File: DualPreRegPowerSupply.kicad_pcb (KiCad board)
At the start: 4 copper layers, 100 x 100 mm, 178 parts, among them J101 Banana_Red, J102 Banana_Black, J201 Banana_Red, J202 Banana_Black, J401 Conn_02x05_Odd_Even, J601 Power Input, J801 Conn_01x03_Pin, J802 Conn_02x02_Odd_Even, J901 Power Input, M401 Fan_4pin, Q301 MMBT3904, Q302 TIP42C, Q303 BSS138, Q401 BSS138, Q501 MMBT3906, Q801 BSS138, Q802 BSS138, U1001 AP64060QWU, U1002 AP7383, U1003 LM2776, U1005 XC6901D121MR-G, U301 TLV4387PWR, U302 LMV331, U501 LT8612, U701 ADS1118IDGS, U702 MCP48FVB22, U801 ISO6721RFBD, U802 ATtiny1614-SS, U901 AP63200WU

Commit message: test commit
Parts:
- removed the Q302 at (137.1, 126.6)

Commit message: test commit 2
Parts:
- moved TP504 15.1 mm to (103.2, 68.2)
- moved TP602 5.25 mm to (102.6, 82.6)
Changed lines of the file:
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@@
 	(footprint "LibEigen:SMD Test Point PCWCTE"
 		(layer "B.Cu")
-		(at 97.6 84.1 90)
+		(at 102.625 82.575 90)
 		(property "Reference" "TP602"
 			(at 0 1.9 270)
@@
 	(footprint "LibEigen:SMD Test Point PCWCTE"
 		(layer "B.Cu")
-		(at 92.6 57.5 -90)
+		(at 103.225 68.175 -90)
 		(property "Reference" "TP504"
 			(at 0 1.9 90)

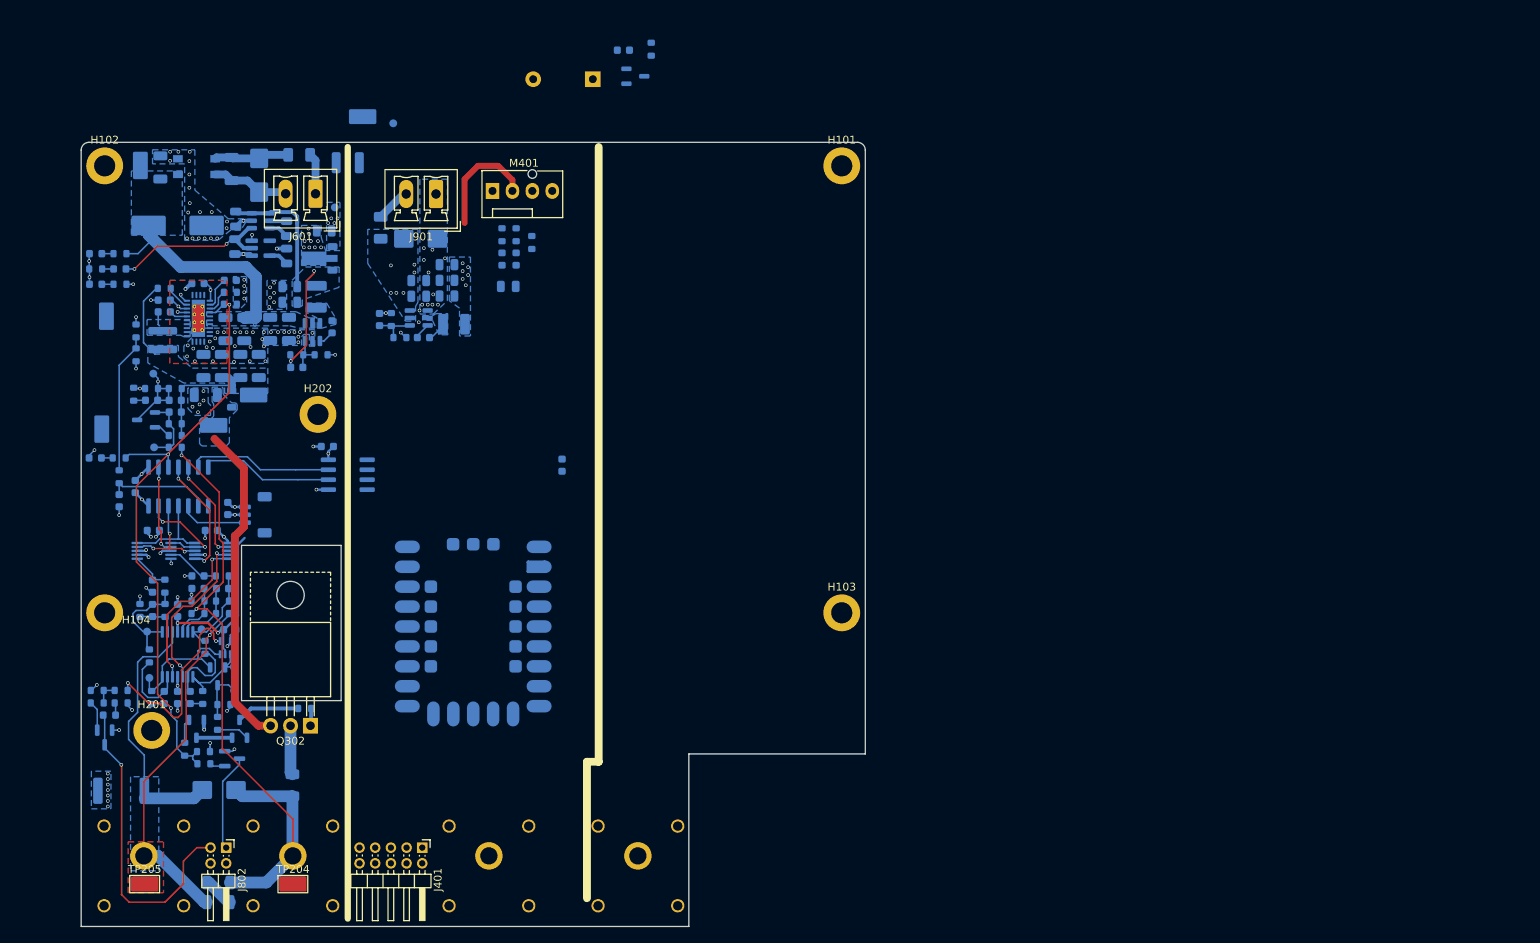
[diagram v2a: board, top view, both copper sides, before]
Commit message: changed pass element drive
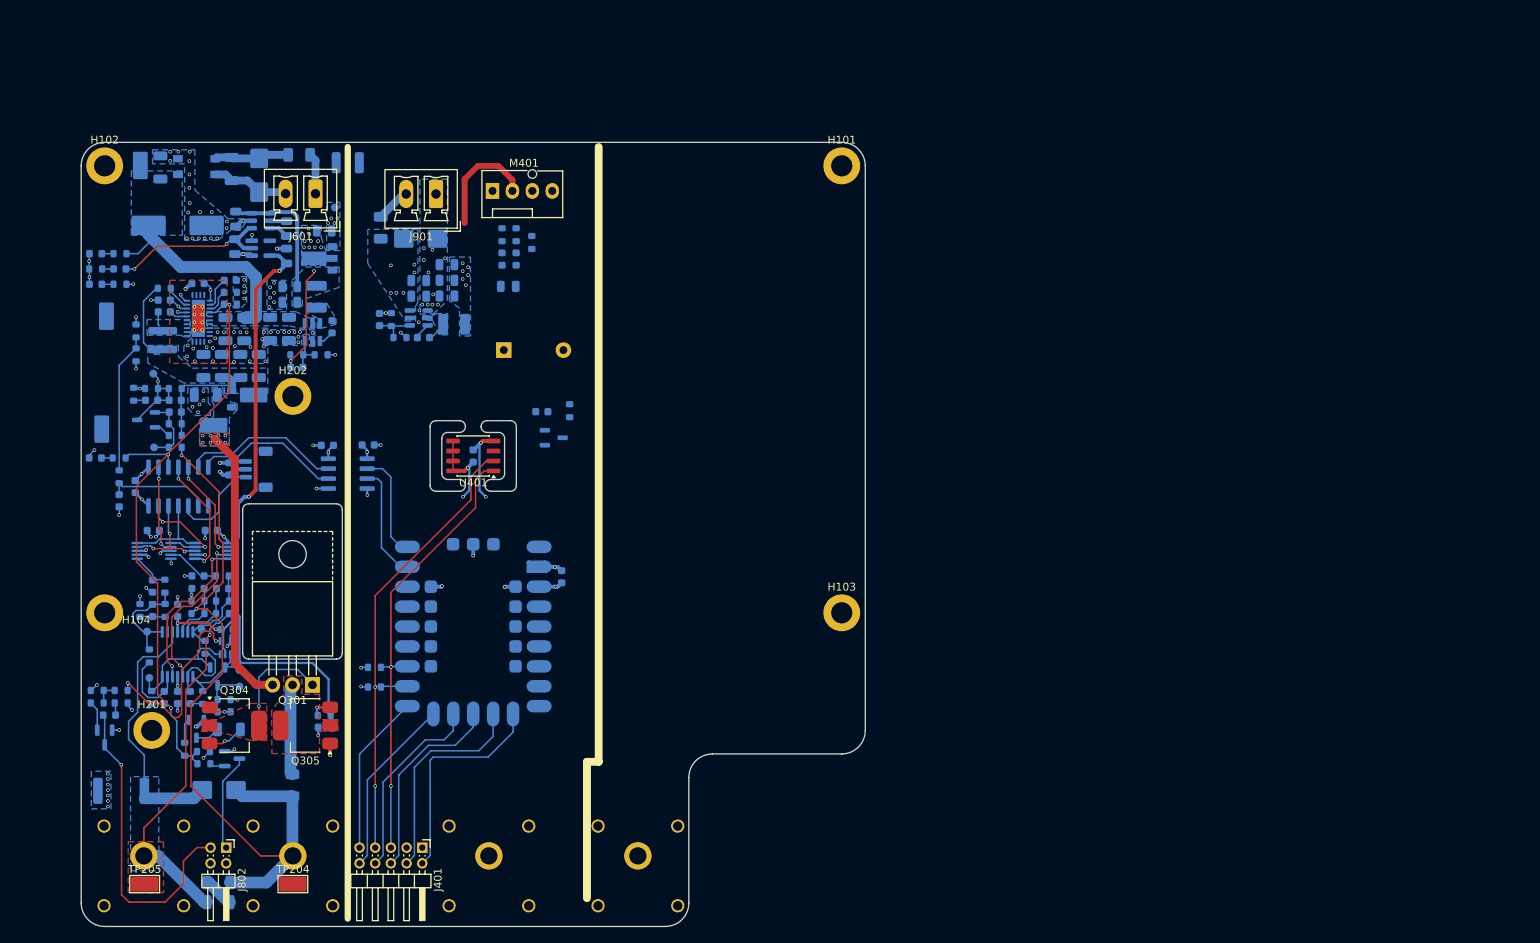
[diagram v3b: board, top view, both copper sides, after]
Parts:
- removed Q302: TIP42C, Package_TO_SOT_THT:TO-220-3_Horizontal_TabUp
- removed R311: 100, Resistor_SMD:R_0603_1608Metric
- removed TP201: TestPoint, LibEigen:SMD Test Point PCWCTE
- removed TP202: TestPoint_Alt, TestPoint:TestPoint_Pad_D1.0mm
- added C309: 100n, Capacitor_SMD:C_0603_1608Metric, B.Cu at (131.0, 120.6)
- added C404: 100n, Capacitor_SMD:C_0603_1608Metric, B.Cu at (150.0, 86.0)
- added C805: 100n, Capacitor_SMD:C_0603_1608Metric, B.Cu at (136.6, 84.6)
- added Q304: BCP56, Package_TO_SOT_SMD:SOT-223, F.Cu at (119.5, 120.4)
- added Q305: BCP56, Package_TO_SOT_SMD:SOT-223, F.Cu at (128.6, 120.4)
- added R320: 47, Resistor_SMD:R_0603_1608Metric, B.Cu at (131.0, 119.1)
- added R321: 150, Resistor_SMD:R_1206_3216Metric, B.Cu at (118.8, 120.9)
- added R403: 2k, Resistor_SMD:R_0603_1608Metric, B.Cu at (137.4, 113.0)
- added R404: 2k, Resistor_SMD:R_0603_1608Metric, B.Cu at (137.4, 115.5)
- added U401: TMP1075D, Package_SO:SO-8_3.9x4.9mm_P1.27mm, F.Cu at (150.0, 86.0)
- C303: value 10n -> 1n
- Q301: value MMBT3904 -> TIP125; footprint Package_TO_SOT_SMD:SOT-23-3 -> Package_TO_SOT_THT:TO-220-3_Horizontal_TabUp; moved to F.Cu
- R310: value 1k -> 0
- moved C402 47.3 mm to (158.8, 80.3)
- moved Q401 47.3 mm to (160.3, 83.7)
- moved R401 47.3 mm to (162.3, 80.2)
- moved BZ401 36.4 mm to (153.9, 72.5), turned to 0 degrees
- moved C401 14.2 mm to (161.3, 101.4)
- moved Q301 10.9 mm to (129.5, 115.2), turned to 180 degrees
- moved J801 5.80 mm to (122.3, 87.7)
- moved C803 5.05 mm to (118.8, 87.7)
- moved H202 3.94 mm to (127.0, 78.4)
- moved R310 1.69 mm to (118.2, 118.6), turned to 0 degrees
- moved TP306 0.86 mm to (120.2, 115.4)
- moved TP304 0.83 mm to (120.2, 113.3)
- moved R306 0.63 mm to (118.2, 117.1)
- moved C306 0.35 mm to (118.6, 108.1)
- moved C801 0.14 mm to (131.4, 84.7)
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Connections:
- A401 pad 0: unconnected-(A401-GPIO0-Pad0) -> /Ch1Power/Tx_Ctr
- A401 pad 1: /Control/RESET -> /Ch1Power/Rx_Ctr
- A401 pad 10: unconnected-(A401-GPIO10-Pad10) -> /Control/SCK
- A401 pad 11: unconnected-(A401-GPIO11-Pad11) -> /Control/SDI(MOSI)
- A401 pad 12: unconnected-(A401-GPIO12-Pad12) -> /Control/DC
- A401 pad 13: unconnected-(A401-GPIO13-Pad13) -> /Control/CS
- A401 pad 2: /Control/SCK -> unconnected-(A401-GPIO2-Pad2)
- A401 pad 20: /Control/CH2_I2C_SDA -> unconnected-(A401-GPIO20-Pad20)
- A401 pad 21: /Control/CH2_I2C_SCL -> unconnected-(A401-GPIO21-Pad21)
- A401 pad 26: unconnected-(A401-GPIO26_ADC0-Pad26) -> /Control/FanPWM
- A401 pad 27: unconnected-(A401-GPIO27_ADC1-Pad27) -> /Control/Buzzer
- A401 pad 3: /Control/SDI(MOSI) -> unconnected-(A401-GPIO3-Pad3)
- A401 pad 4: /Control/DC -> /Control/Tx_Ch2
- A401 pad 5: /Control/CS -> /Control/Rx_Ch2
- A401 pad 6: /Control/CH1_I2C_SDA -> /Control/SDA
- A401 pad 7: /Control/CH1_I2C_SCL -> /Control/SCL
- A401 pad 8: unconnected-(A401-GPIO8-Pad8) -> /Control/~{INT}
- A401 pad 9: unconnected-(A401-GPIO9-Pad9) -> /Control/RESET
- Q301 pad 1: /Ch1Power/Linear_PostReg/Base -> /Ch1Power/Linear_PostReg/Base_drive
- Q301 pad 2: Net-(Q301-E) -> /Ch1Power/Linear_PostReg/preFuseOut+
- Q301 pad 3: Net-(Q301-C) -> /Ch1Power/Linear_PostReg/PreReg
- Q303 pad 3: Net-(Q301-E) -> Net-(Q303-D)
- U801 pad 1: unconnected-(U801-VCC1-Pad1) -> +3.3V
- U801 pad 2: unconnected-(U801-INA-Pad2) -> /Ch1Power/Tx_Ctr
- U801 pad 3: unconnected-(U801-OUTB-Pad3) -> /Ch1Power/Rx_Ctr
- U801 pad 4: unconnected-(U801-GND1-Pad4) -> GNDD
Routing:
- net CH1_-1.2V: track 27.2 -> 89.3 mm, vias 2 -> 4
- net /Control/SCL: track 0.00 -> 60.2 mm, vias 0 -> 2
- net /Control/SDA: track 0.00 -> 57.6 mm, vias 0 -> 2
- net /Control/CS: track 0.00 -> 27.9 mm
- net /Control/DC: track 0.00 -> 27.2 mm
- net /Control/SDI(MOSI): track 0.00 -> 25.4 mm
- net /Control/SCK: track 0.00 -> 24.6 mm
- net /Control/RESET: track 0.00 -> 23.0 mm
- net /Control/~{INT}: track 0.00 -> 20.6 mm
- net +3.3V: track 1.52 -> 21.0 mm, vias 7 -> 14
- net GNDD: track 0.98 -> 18.9 mm, vias 13 -> 20
- net /Ch1Power/Rx_Ctr: track 0.00 -> 14.6 mm
- net /Ch1Power/Linear_PostReg/Base_drive: track 0.00 -> 14.2 mm, vias 0 -> 1
- net /Ch1Power/Tx_Ctr: track 0.00 -> 13.7 mm
- net Net-(Q301-C): track 8.08 -> 0.00 mm
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- added copper zone on F.Cu, net /Ch1Power/Linear_PostReg/Base_drive
- added copper zone on F.Cu, net /Ch1Power/Linear_PostReg/PreReg
- added copper zone on F.Cu, net /Ch1Power/Linear_PostReg/preFuseOut+
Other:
- outline, holes or cut-outs redrawn

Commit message: added Ch2 and removed global power flags
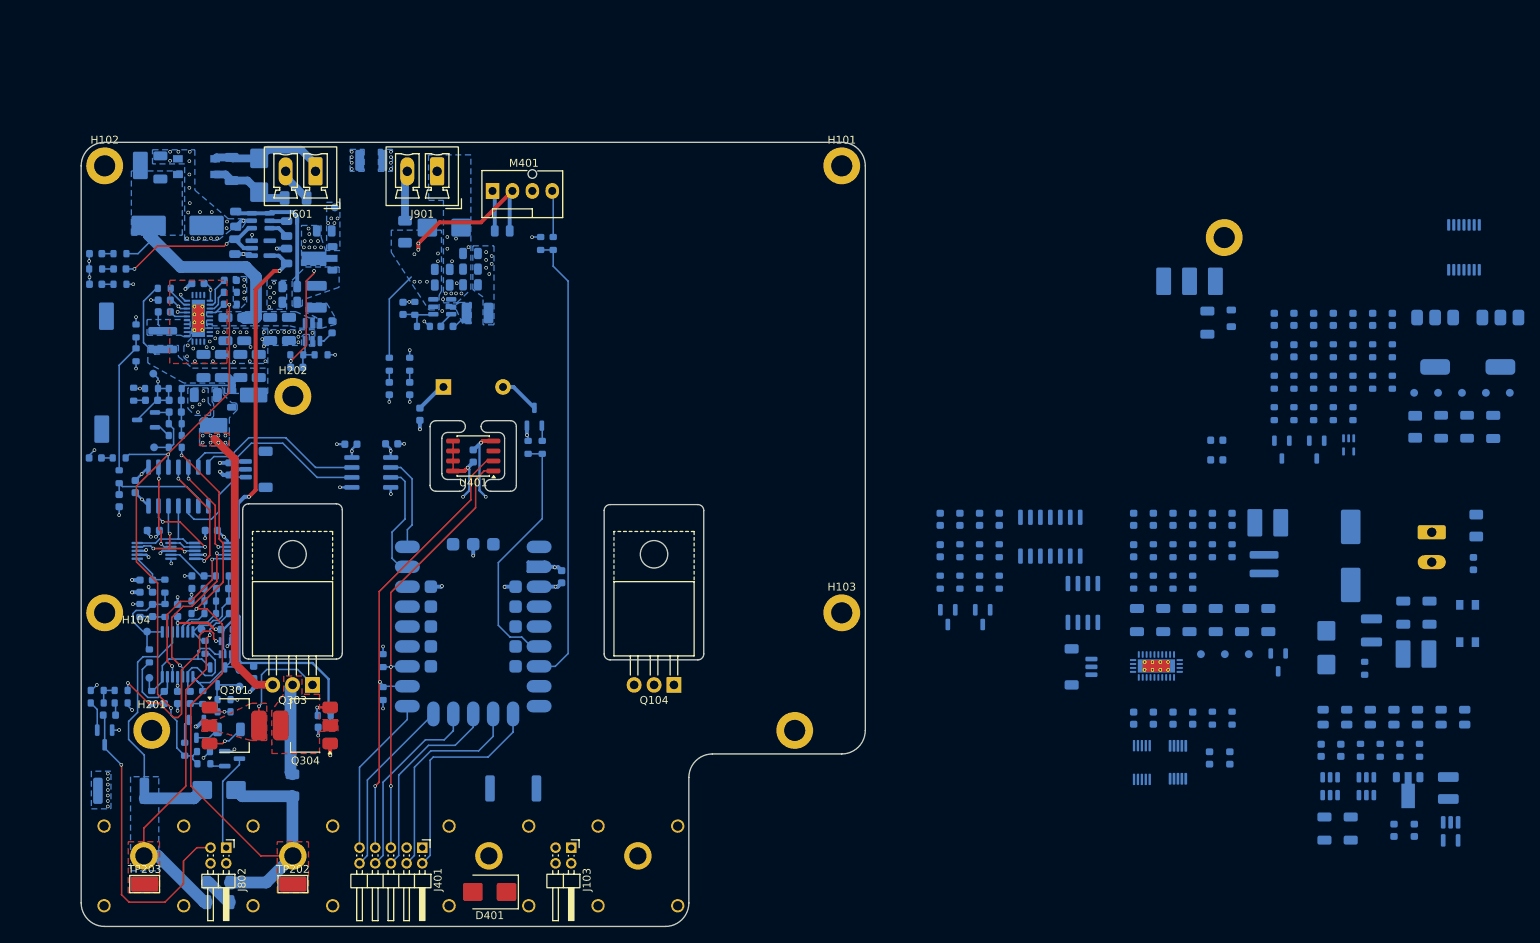
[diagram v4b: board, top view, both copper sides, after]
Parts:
- added C101: 10u, Capacitor_SMD:C_1206_3216Metric, B.Cu at (234.6, 106.9)
- added C1012: 2,2u, Capacitor_SMD:C_0603_1608Metric, B.Cu at (107.5, 102.6)
- added C1013: 2,2u, Capacitor_SMD:C_0603_1608Metric, B.Cu at (122.0, 113.6)
- added C102: 10u, Capacitor_SMD:C_1206_3216Metric, B.Cu at (238.0, 106.9)
- added C103: 100n, Capacitor_SMD:C_0603_1608Metric, B.Cu at (252.2, 68.6)
- added C104: 100n, Capacitor_SMD:C_0603_1608Metric, B.Cu at (254.7, 68.6)
- added C105: 22u, Capacitor_SMD:C_1206_3216Metric, B.Cu at (258.6, 133.5)
- added C106: 100n, Capacitor_SMD:C_0603_1608Metric, B.Cu at (209.6, 94.1)
- added C107: 22u, Capacitor_SMD:C_1206_3216Metric, B.Cu at (261.9, 133.5)
- added C108: 100n, Capacitor_SMD:C_0603_1608Metric, B.Cu at (234.2, 94.1)
- added C109: 100n, Capacitor_SMD:C_0603_1608Metric, B.Cu at (212.1, 94.1)
- added C110: 1u, Capacitor_SMD:C_0603_1608Metric, B.Cu at (236.7, 94.1)
- added C111: 1n, Capacitor_SMD:C_0603_1608Metric, B.Cu at (257.2, 68.6)
- added C112: 100p, Capacitor_SMD:C_0603_1608Metric, B.Cu at (259.7, 68.6)
- added C113: ##, Capacitor_SMD:C_0603_1608Metric, B.Cu at (234.2, 119.4)
- added C114: ##, Capacitor_SMD:C_0603_1608Metric, B.Cu at (236.7, 119.4)
- added C115: 100n, Capacitor_SMD:C_0603_1608Metric, B.Cu at (258.1, 123.5)
- added C116: 56p, Capacitor_SMD:C_0603_1608Metric, B.Cu at (260.6, 123.5)
- added C117: 100n, Capacitor_SMD:C_0603_1608Metric, B.Cu at (214.6, 94.1)
- added C118: 100n, Capacitor_SMD:C_0603_1608Metric, B.Cu at (239.2, 94.1)
- added C119: opt, Capacitor_SMD:C_0603_1608Metric, B.Cu at (241.8, 94.1)
- added C120: 10u, Capacitor_SMD:C_1206_3216Metric, B.Cu at (268.6, 106.0)
- added C1201: 2,2u, Capacitor_SMD:C_0603_1608Metric, B.Cu at (244.8, 84.0)
- added C1202: 2,2u, Capacitor_SMD:C_0603_1608Metric, B.Cu at (244.8, 86.5)
- added C121: 10p, Capacitor_SMD:C_0603_1608Metric, B.Cu at (262.2, 68.6)
- added C122: 1u, Capacitor_SMD:C_0603_1608Metric, B.Cu at (217.1, 94.1)
- added C123: 1u, Capacitor_SMD:C_0603_1608Metric, B.Cu at (244.3, 94.1)
- added C124: 22u, Capacitor_SMD:C_0805_2012Metric, B.Cu at (258.4, 119.3)
- added C125: CHV1210N1K0103KXT, Capacitor_SMD:C_1210_3225Metric, B.Cu at (264.6, 108.2)
- added C126: 100n, Capacitor_SMD:C_0603_1608Metric, B.Cu at (239.2, 119.4)
- added C127: 10u, Capacitor_SMD:C_0805_2012Metric, B.Cu at (261.4, 119.3)
- added C128: 100n, Capacitor_SMD:C_0603_1608Metric, B.Cu at (241.8, 119.4)
- added C129: 1n, Capacitor_SMD:C_0603_1608Metric, B.Cu at (246.8, 94.1)
- added C130: 10p, Capacitor_SMD:C_0603_1608Metric, B.Cu at (264.7, 68.6)
- added C131: 22u, Capacitor_SMD:C_0805_2012Metric, B.Cu at (264.4, 119.3)
- added C132: 100n, Capacitor_SMD:C_0603_1608Metric, B.Cu at (267.2, 68.6)
- added C133: 1u, Capacitor_SMD:C_0805_2012Metric, B.Cu at (267.4, 119.3)
- added C134: 10p, Capacitor_SMD:C_0603_1608Metric, B.Cu at (252.2, 72.6)
- added C135: 10u, Capacitor_SMD:C_1206_3216Metric, B.Cu at (272.0, 106.0)
- added C136: 10u, Capacitor_SMD:C_1206_3216Metric, B.Cu at (241.3, 106.9)
- added C137: opt, Capacitor_SMD:C_0603_1608Metric, B.Cu at (234.2, 98.1)
- added C138: 22u, Capacitor_SMD:CP_Elec_8x10.5, B.Cu at (261.9, 98.7)
- added C139: 10u, Capacitor_SMD:C_0805_2012Metric, B.Cu at (270.4, 119.3)
- added C140: 10u, Capacitor_SMD:C_1206_3216Metric, B.Cu at (244.7, 106.9)
- added C141: 10u, Capacitor_SMD:C_1206_3216Metric, B.Cu at (248.0, 106.9)
- added C142: 10u, Capacitor_SMD:C_0805_2012Metric, B.Cu at (273.4, 119.3)
- added C143: 10u, Capacitor_SMD:C_1206_3216Metric, B.Cu at (251.4, 106.9)
- added C144: 100n, Capacitor_SMD:C_0603_1608Metric, B.Cu at (209.6, 98.1)
- added C145: 10u, Capacitor_SMD:C_1206_3216Metric, B.Cu at (280.1, 82.3)
- added C146: 10u, Capacitor_SMD:C_0805_2012Metric, B.Cu at (276.4, 119.3)
- added C147: 100n, Capacitor_SMD:C_0603_1608Metric, B.Cu at (254.7, 72.6)
- added C405: 10u, Capacitor_SMD:C_1206_3216Metric, B.Cu at (243.6, 69.0)
- added D101: SM6T36A, Diode_SMD:D_SMB, B.Cu at (258.8, 110.5)
- added D102: BAT54A, Package_TO_SOT_SMD:SOT-23-3, B.Cu at (253.1, 85.2)
- added D103: LED 3V3, LED_SMD:LED_0603_1608Metric, B.Cu at (243.9, 124.5)
- added D104: LED 40V, LED_SMD:LED_0603_1608Metric, B.Cu at (277.6, 99.7)
- added D105: LED 3V3, LED_SMD:LED_0603_1608Metric, B.Cu at (267.4, 133.7)
- added D106: LED -5V, LED_SMD:LED_0603_1608Metric, B.Cu at (270.0, 133.7)
- added D107: LED 3V3, LED_SMD:LED_0603_1608Metric, B.Cu at (246.5, 124.5)
- added D401: SM6T36A, Diode_SMD:D_SMB, F.Cu at (152.1, 141.6)
- added F101: 3,5A, Fuse:Fuse_1206_3216Metric, B.Cu at (277.9, 94.9)
- added F102: Fuse, Fuse:Fuse_1206_3216Metric, B.Cu at (270.1, 82.3)
- added FL101: ACM4520-901-2P-T000, LibEigen:ACM4520_TDK, B.Cu at (276.8, 107.4)
- added H401: M2,5, MountingHole:MountingHole_2.7mm_M2.5_DIN965_Pad, B.Cu at (191.0, 121.0)
- added H402: M2,5, MountingHole:MountingHole_2.7mm_M2.5_DIN965_Pad, B.Cu at (245.8, 58.1)
- added J103: Conn_02x02_Odd_Even, Connector_PinHeader_2.00mm:PinHeader_2x02_P2.00mm_Horizontal, F.Cu at (162.5, 135.9)
- added J402: Banana_Red, Connector:Banana_Cliff_FCR7350R_S16N-PC_Horizontal, B.Cu at (171.0, 137.0)
- added J403: Banana_Black, Connector:Banana_Cliff_FCR7350B_S16N-PC_Horizontal, B.Cu at (152.0, 137.0)
- added L101: 10u CBC3225T100KR, Inductor_SMD:L_1210_3225Metric, B.Cu at (274.4, 128.3)
- added L102: 10u 74438357100, Inductor_SMD:L_Wuerth_MAPI-4030, B.Cu at (250.9, 99.8)
- added L401: 1u, Inductor_SMD:L_0805_2012Metric, B.Cu at (246.7, 68.4)
- added Q101: MMBT3906, Package_TO_SOT_SMD:SOT-23-3, B.Cu at (252.7, 112.3)
- added Q102: BCP56, Package_TO_SOT_SMD:SOT-223, B.Cu at (272.7, 71.5)
- added Q103: BSS138, Package_TO_SOT_SMD:SOT-23-3, B.Cu at (257.6, 85.2)
- added Q104: TIP125, Package_TO_SOT_THT:TO-220-3_Horizontal_TabUp, F.Cu at (175.6, 115.2)
- added Q105: BSS138, Package_TO_SOT_SMD:SOT-23, B.Cu at (210.5, 106.6)
- added Q106: BSS138, Package_TO_SOT_SMD:SOT-23, B.Cu at (215.0, 106.6)
- added Q107: BCP56, Package_TO_SOT_SMD:SOT-223, B.Cu at (281.0, 71.5)
- added R101: 10k, Resistor_SMD:R_0603_1608Metric, B.Cu at (236.7, 98.1)
- added R102: 10k, Resistor_SMD:R_0603_1608Metric, B.Cu at (257.2, 72.6)
- added R103: 10k, Resistor_SMD:R_0603_1608Metric, B.Cu at (259.7, 72.6)
- added R104: ##, Resistor_SMD:R_0603_1608Metric, B.Cu at (244.3, 119.4)
- added R105: ##, Resistor_SMD:R_0603_1608Metric, B.Cu at (246.8, 119.4)
- added R106: 1k, Resistor_SMD:R_0603_1608Metric, B.Cu at (262.2, 72.6)
- added R107: 0, Resistor_SMD:R_0603_1608Metric, B.Cu at (264.7, 72.6)
- added R108: 60,4k, Resistor_SMD:R_0603_1608Metric, B.Cu at (239.2, 98.1)
- added R109: 10k, Resistor_SMD:R_0603_1608Metric, B.Cu at (212.1, 98.1)
- added R110: opt, Resistor_SMD:R_0603_1608Metric, B.Cu at (241.8, 98.1)
- added R111: 49,9k, Resistor_SMD:R_0603_1608Metric, B.Cu at (244.3, 98.1)
- added R112: 1,2k, Resistor_SMD:R_0603_1608Metric, B.Cu at (267.2, 72.6)
- added R113: 10k, Resistor_SMD:R_0603_1608Metric, B.Cu at (214.6, 98.1)
- added R114: 115k, Resistor_SMD:R_0603_1608Metric, B.Cu at (263.2, 123.5)
- added R115: 22,1k, Resistor_SMD:R_0603_1608Metric, B.Cu at (265.7, 123.5)
- added R116: 4,3k, Resistor_SMD:R_0603_1608Metric, B.Cu at (252.2, 76.6)
- added R117: 3,3k, Resistor_SMD:R_0603_1608Metric, B.Cu at (254.7, 76.6)
- added R118: 1k, Resistor_SMD:R_0603_1608Metric, B.Cu at (257.2, 76.6)
- added R119: 4,3k, Resistor_SMD:R_0603_1608Metric, B.Cu at (259.7, 76.6)
- added R120: 10k, Resistor_SMD:R_0603_1608Metric, B.Cu at (262.2, 76.6)
- added R121: 0, Resistor_SMD:R_0603_1608Metric, B.Cu at (264.7, 76.6)
- added R122: opt, Resistor_SMD:R_0603_1608Metric, B.Cu at (246.8, 98.1)
- added R123: 220, Resistor_SMD:R_0603_1608Metric, B.Cu at (267.2, 76.6)
- added R124: 2,4k, Resistor_SMD:R_0603_1608Metric, B.Cu at (217.1, 98.1)
- added R125: 1k, Resistor_SMD:R_0603_1608Metric, B.Cu at (234.2, 102.1)
- added R126: 4,99k, Resistor_SMD:R_0603_1608Metric, B.Cu at (236.7, 102.1)
- added R127: 62k, Resistor_SMD:R_0603_1608Metric, B.Cu at (252.2, 80.6)
- added R128: 62k, Resistor_SMD:R_0603_1608Metric, B.Cu at (254.7, 80.6)
- added R129: 150, Resistor_SMD:R_1206_3216Metric, B.Cu at (273.4, 82.3)
- added R130: 100k, Resistor_SMD:R_0603_1608Metric, B.Cu at (239.2, 102.1)
- added R131: 18k, Resistor_SMD:R_0603_1608Metric, B.Cu at (257.2, 80.6)
- added R132: 1,6k, Resistor_SMD:R_0603_1608Metric, B.Cu at (259.7, 80.6)
- added R133: 100k, Resistor_SMD:R_0603_1608Metric, B.Cu at (241.8, 102.1)
- added R134: 38k, Resistor_SMD:R_0603_1608Metric, B.Cu at (263.7, 113.1)
- added R135: 1k, Resistor_SMD:R_0603_1608Metric, B.Cu at (209.6, 102.1)
- added R136: 2,4k, Resistor_SMD:R_0603_1608Metric, B.Cu at (268.2, 123.5)
- added R137: 1k, Resistor_SMD:R_0603_1608Metric, B.Cu at (212.1, 102.1)
- added R138: 100m, Resistor_SMD:R_2512_6332Metric, B.Cu at (155.1, 128.4)
- added R139: ###, Resistor_SMD:R_0603_1608Metric, B.Cu at (270.7, 123.5)
- added R140: 2,4k, Resistor_SMD:R_0603_1608Metric, B.Cu at (214.6, 102.1)
- added R141: 200m, Resistor_SMD:R_1206_3216Metric, B.Cu at (276.7, 82.3)
- added R142: 47, Resistor_SMD:R_0603_1608Metric, B.Cu at (262.2, 80.6)
- added R201: 10k, Resistor_SMD:R_0603_1608Metric, B.Cu at (157.0, 84.9)
- added R202: 10k, Resistor_SMD:R_0603_1608Metric, B.Cu at (158.6, 58.9)
- added TH101: NCU18XH103F60RB, Resistor_SMD:R_0603_1608Metric, B.Cu at (217.1, 102.1)
- added TP101: Vsense, TestPoint:TestPoint_Pad_D1.0mm, B.Cu at (270.0, 77.9)
- added TP102: CV_loop, TestPoint:TestPoint_Pad_D1.0mm, B.Cu at (273.0, 77.9)
- added TP103: CC_loop, TestPoint:TestPoint_Pad_D1.0mm, B.Cu at (276.1, 77.9)
- added TP104: CC/CV, TestPoint:TestPoint_Pad_D1.0mm, B.Cu at (279.1, 77.9)
- added TP105: Isense, TestPoint:TestPoint_Pad_D1.0mm, B.Cu at (282.2, 77.9)
- added TP106: TestPoint_Alt, TestPoint:TestPoint_Pad_D1.0mm, B.Cu at (242.8, 111.3)
- added TP107: TestPoint_Alt, TestPoint:TestPoint_Pad_D1.0mm, B.Cu at (245.9, 111.3)
- added TP108: TestPoint, LibEigen:SMD Test Point PCWCTE, B.Cu at (268.6, 111.3)
- added TP109: TestPoint, LibEigen:SMD Test Point PCWCTE, B.Cu at (271.9, 111.3)
- added TP110: TestPoint_Alt, TestPoint:TestPoint_Pad_D1.0mm, B.Cu at (248.9, 111.3)
- added TP111: TestPoint, LibEigen:SMD Test Point PCWCTE, B.Cu at (249.7, 94.5)
- added TP112: TestPoint, LibEigen:SMD Test Point PCWCTE, B.Cu at (253.0, 94.5)
- added TP401: TestPoint, LibEigen:SMD Test Point PCWCTE, B.Cu at (238.1, 63.7)
- added TP402: TestPoint, LibEigen:SMD Test Point PCWCTE, B.Cu at (241.3, 63.7)
- added TP403: TestPoint, LibEigen:SMD Test Point PCWCTE, B.Cu at (244.7, 63.7)
- added U101: TLV4387PWR, Package_SO:TSSOP-14_4.4x5mm_P0.65mm, B.Cu at (276.4, 59.4)
- added U102: ISO6721RFBD, Package_SO:SOIC-8_3.9x4.9mm_P1.27mm, B.Cu at (227.8, 104.7)
- added U103: AP64060QWU, Package_TO_SOT_SMD:TSOT-23-6, B.Cu at (259.3, 128.1)
- added U104: LT8612, Package_DFN_QFN:QFN-28-1EP_3x6mm_P0.5mm_EP1.7x4.75mm_ThermalVias, B.Cu at (237.1, 112.8)
- added U105: LMV331, Package_TO_SOT_SMD:SOT-353_SC-70-5, B.Cu at (261.6, 84.6)
- added U106: ATtiny1614-SS, Package_SO:SOIC-14_3.9x8.7mm_P1.27mm, B.Cu at (223.6, 96.3)
- added U107: ADS1118IDGS, Package_SO:TSSOP-10_3x3mm_P0.5mm, B.Cu at (235.3, 125.1)
- added U108: MCP48FVB22, Package_SO:MSOP-10_3x3mm_P0.5mm, B.Cu at (239.9, 125.1)
- added U109: AP7383, Package_TO_SOT_SMD:SOT-89-3, B.Cu at (269.2, 128.9)
- added U110: LM2776, Package_TO_SOT_SMD:SOT-23-6, B.Cu at (263.9, 128.1)
- added U111: XC6901D121MR-G, Package_TO_SOT_SMD:SC-74A-5_1.55x2.9mm_P0.95mm, B.Cu at (274.6, 133.9)
- J101: value Banana_Red -> Power Input; footprint Connector:Banana_Cliff_FCR7350R_S16N-PC_Horizontal -> Connector_Phoenix_MC:PhoenixContact_MCV_1,5_2-G-3.81_1x02_P3.81mm_Vertical
- J102: value Banana_Black -> Conn_01x03_Pin; footprint Connector:Banana_Cliff_FCR7350B_S16N-PC_Horizontal -> Connector_JST:JST_SH_BM03B-SRSS-TB_1x03-1MP_P1.00mm_Vertical
- moved J101 109.3 mm to (272.2, 95.7), turned to -90 degrees
- moved J102 79.3 mm to (227.5, 112.9), turned to -90 degrees
- moved D902 23.1 mm to (139.3, 77.4)
- moved R901 23.1 mm to (139.3, 74.3)
- moved D903 20.3 mm to (141.9, 77.4)
- moved R904 20.3 mm to (141.9, 74.3)
- moved C403 15.6 mm to (143.2, 80.7), turned to -90 degrees
- moved BZ401 9.02 mm to (146.2, 77.2)
- moved C404 7.12 mm to (153.7, 57.3), turned to 180 degrees
- moved R403 5.84 mm to (158.8, 84.9), turned to 90 degrees
- moved F601 5.52 mm to (127.3, 53.1)
- moved Q401 3.64 mm to (157.8, 81.0), turned to 90 degrees
- moved C901 3.32 mm to (146.1, 62.2)
- moved C902 3.32 mm to (146.1, 64.2)
- moved C903 3.32 mm to (146.7, 69.5)
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- renumbered C1011 to C1001, C1001 to C1002, C1002 to C1003, C1003 to C1004, C1004 to C1005, C1008 to C1006, C1005 to C1007, C1009 to C1008, C1007 to C1009, C1012 to C1011, C307 to C306, C306 to C307, C310 to C309, C309 to C310, C404 to C401, C401 to C402, C402 to C403, C403 to C404, C604 to C602, C602 to C603, C603 to C604, C805 to C801, C801 to C802, C802 to C803, C803 to C805, D1002 to D1001, D1003 to D1002, Q304 to Q301, Q303 to Q302, Q301 to Q303, Q305 to Q304, Q802 to Q801, Q801 to Q802, R1004 to R1003, R1005 to R1004, R319 to R305, R305 to R306, R318 to R307, R306 to R308, R307 to R309, R314 to R310, R310 to R311, R317 to R312, R308 to R313, R309 to R314, R321 to R315, R312 to R316, R313 to R317, R315 to R318, R316 to R319, R403 to R401, R404 to R402, R401 to R403, R402 to R404, R806 to R802, R802 to R803, R803 to R805, R805 to R806, TP203 to TP201, TP204 to TP202, TP205 to TP203, TP303 to TP301, TP304 to TP302, TP305 to TP303, TP306 to TP304, TP302 to TP305, U1005 to U1004
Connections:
- net +40V1 renamed +40VCh1
- net CH1_+3.3V renamed +3V3Ch1
- net CH1_-1.2V renamed -1V2Ch1
- net GND1 renamed GND_Ch1
- A401 pad 4: /Control/Tx_Ch2 -> /Ch1Power1/Tx_Ctr
- A401 pad 5: /Control/Rx_Ch2 -> /Ch1Power1/Rx_Ctr
- C601 pad 1: /Ch1Power/Input/Input+ -> /Ch1Power/Input/Input_Fused+
- C601 pad 2: Net-(D601-A2) -> /Ch1Power/Input/Input-
- D601 pad 1: /Ch1Power/Input/Input+ -> /Ch1Power/Input/Input_Fused+
- D601 pad 2: Net-(D601-A2) -> /Ch1Power/Input/Input-
- F601 pad 1: /Ch1Power/Input/Input- -> /Ch1Power/Input/Input+
- F601 pad 2: Net-(D601-A2) -> /Ch1Power/Input/Input_Fused+
- FL601 pad 1: Net-(D601-A2) -> /Ch1Power/Input/Input-
- FL601 pad 2: /Ch1Power/Input/Input+ -> /Ch1Power/Input/Input_Fused+
- J101 pad 1: unconnected-(J101-Pin_1-Pad1) -> /Ch1Power1/Input/Input-
- J102 pad 1: unconnected-(J102-Pin_1-Pad1) -> /Ch1Power1/MCU/UPDI
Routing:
- net /Control/FanPWM: track 0.00 -> 58.2 mm
- net /Control/Buzzer: track 0.00 -> 32.3 mm
- net +12V: track 14.9 -> 32.6 mm, vias 6 -> 8
- net GNDD: track 18.9 -> 30.3 mm, vias 20 -> 29
- net /Ch1Power/Input/Input_Fused+: track 0.00 -> 10.1 mm
- net /Ch1Power/Input/Input-: track 5.24 -> 15.1 mm
- net Net-(D601-A2): track 9.62 -> 0.00 mm
- net Net-(M401-PWM): track 0.00 -> 5.92 mm
- net /Ch1Power/Input/Input+: track 10.0 -> 4.51 mm
- net +3.3V: track 21.0 -> 26.4 mm, vias 14 -> 15
- net Net-(BZ401--): track 0.00 -> 5.10 mm
- net /Ch1Power/MCU/Rx: track 20.3 -> 23.3 mm
- net /Ch1Power/MCU/Tx: track 18.8 -> 21.8 mm
- net GND_Ch1: track 46.6 -> 49.4 mm, vias 115 -> 121
- net Net-(J901-Pin_2): track 4.46 -> 6.42 mm
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- added copper zone on In1.Cu, net +3V3Ch2
- added copper zone on F.Cu, net /Ch1Power/Linear_PostReg/OUT+
- added copper zone on In2.Cu, net GND_Ch2
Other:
- outline, holes or cut-outs redrawn
- board text added: "Ch1"

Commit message: channel 2
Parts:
- J101: moved to F.Cu
- moved TP108 118.7 mm to (167.4, 49.2)
- moved C125 117.9 mm to (163.0, 48.3), turned to 0 degrees
- moved FL101 117.3 mm to (175.0, 49.0), turned to 180 degrees
- moved C135 116.4 mm to (170.4, 49.0), turned to 90 degrees
- moved TP109 112.1 mm to (186.8, 38.2)
- moved C120 105.7 mm to (179.5, 49.1), turned to 90 degrees
- moved C138 101.5 mm to (169.8, 56.2), turned to 180 degrees
- moved F101 99.0 mm to (187.9, 53.5), turned to 180 degrees
- moved D101 96.8 mm to (183.1, 50.0)
- moved J101 93.8 mm to (190.6, 49.7), turned to 180 degrees
- moved R134 90.2 mm to (207.3, 42.6)
- moved L102 89.1 mm to (167.2, 69.3)
- moved D104 88.5 mm to (207.4, 45.8)
- moved C143 87.0 mm to (171.4, 72.6), turned to 90 degrees
- moved TP106 85.3 mm to (165.3, 75.6)
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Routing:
- net /Ch1Power1/DCDCTracking/SW_OUT: track 0.00 -> 10.5 mm
- net Net-(U104-INT_Vcc): track 0.00 -> 8.38 mm, vias 0 -> 2
- net GND_Ch2: track 0.00 -> 4.83 mm, vias 0 -> 33
- net Net-(U104-TR/SS): track 0.00 -> 4.11 mm
- net Net-(U104-RT): track 0.00 -> 3.14 mm
- net /Ch1Power1/DCDCTracking/Enable: track 0.00 -> 3.03 mm, vias 0 -> 1
- net Net-(U104-PG): track 0.00 -> 2.51 mm
- net /Ch1Power1/DCDCTracking/SW: track 0.00 -> 2.10 mm
- net +3V3Ch2: track 0.00 -> 2.09 mm, vias 0 -> 1
- net /Ch1Power1/DCDCTracking/BST: track 0.00 -> 1.88 mm
- net /Ch1Power1/DCDCTracking/DCDC_FB: track 0.00 -> 0.71 mm, vias 0 -> 1
- net +12V: vias 8 -> 2
- added copper zone on B.Cu, net +40VCh2
- added copper zone on B.Cu, net /Ch1Power1/DCDCTracking/SW
- added copper zone on B.Cu, net /Ch1Power1/DCDCTracking/SW_OUT
- added copper zone on B.Cu, net GND_Ch2

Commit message: routing
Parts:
- removed C1004, C116: 56p, Capacitor_SMD:C_0603_1608Metric
- removed U1001, U103: AP64060QWU, Package_TO_SOT_SMD:TSOT-23-6
- added U1501: LMR51606, Package_TO_SOT_SMD:SOT-23-6, B.Cu at (259.6, 128.1)
- added U601: LMR51606, Package_TO_SOT_SMD:SOT-23-6, B.Cu at (129.5, 70.2)
- L1001, L101: value 10u CBC3225T100KR -> 33u VLS6045EX-330M; footprint Inductor_SMD:L_1210_3225Metric -> Inductor_SMD:L_TDK_VLS6045EX_VLS6045AF
- R1001, R114: value 115k -> 75k
- R1002, R115: value 22,1k -> 16,2k
- moved J102 10.5 mm to (221.7, 104.2)
- moved C1007 8.90 mm to (135.4, 63.0), turned to -90 degrees
- moved C1009 2.83 mm to (132.5, 54.9)
- moved TP501 2.83 mm to (133.8, 51.9)
- moved U1002 2.83 mm to (131.6, 58.4)
- moved C1005 1.90 mm to (126.7, 64.5), turned to -90 degrees
- moved L1001 1.35 mm to (131.0, 64.8)
- moved C1003 0.17 mm to (132.0, 69.7)
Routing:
- net Net-(U601-FB): track 4.93 -> 3.38 mm
- net /Ch1Power/Power/5V: track 32.1 -> 33.1 mm
- net GND_Ch2: vias 33 -> 32
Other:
- board text added: "+"
- board text added: "-"
